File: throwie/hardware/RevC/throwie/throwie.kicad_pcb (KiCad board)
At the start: 2 copper layers, 33.8 x 18.8 mm, 24 parts, among them J1 CONN, Q1 2SC3356, Q2 SS8050-G, T1 TestPoints, T2 TestPoints, T3 TestPoints, T4 TestPoints, U1 C8051F850-A-GU, U2 MIC5231-3.3YM5-TR, X1 RO3101

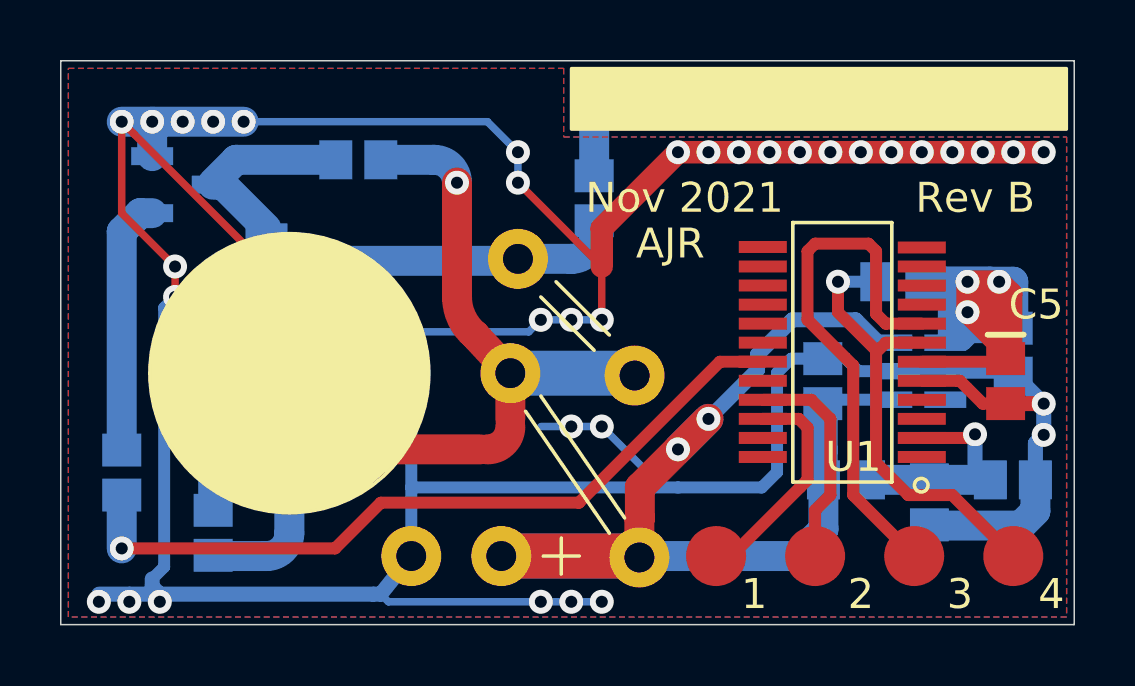
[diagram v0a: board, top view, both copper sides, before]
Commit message: added more test points
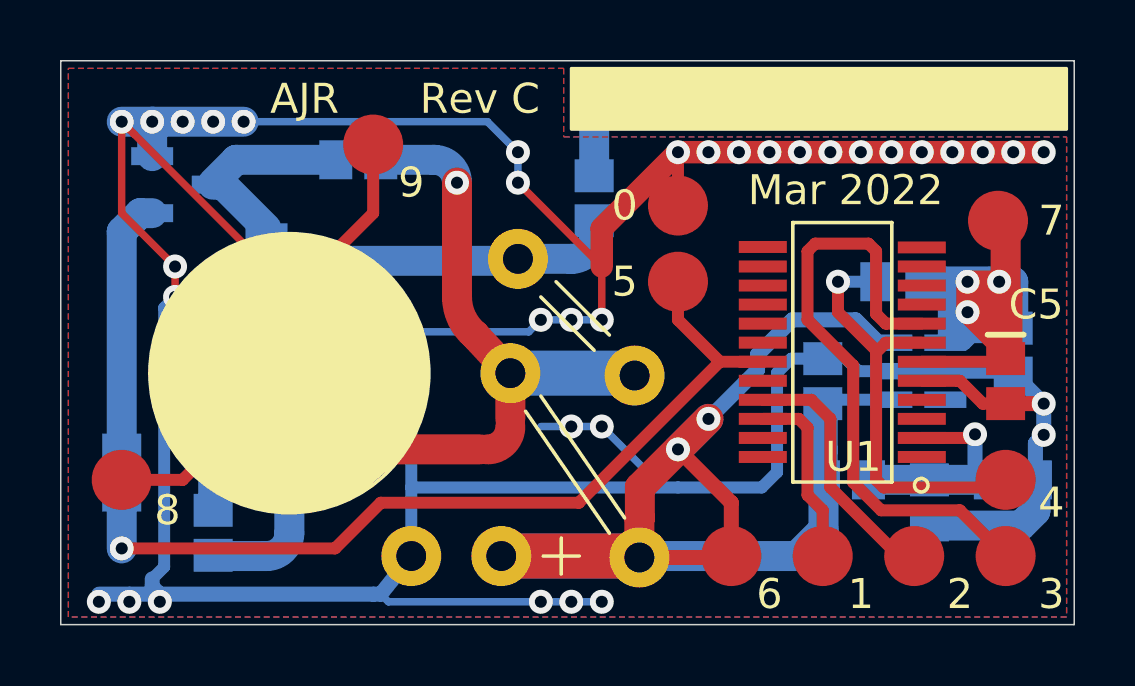
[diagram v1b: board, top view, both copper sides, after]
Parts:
- added T0: TestPoints, throwie:TestPoint, F.Cu at (41.1, 149.4)
- added T5: TestPoints, throwie:TestPoint, F.Cu at (41.1, 151.9)
- added T6: TestPoints, throwie:TestPoint, F.Cu at (42.9, 161.0)
- added T7: TestPoints, throwie:TestPoint, F.Cu at (51.8, 149.9)
- added T8: TestPoints, throwie:TestPoint, F.Cu at (22.6, 158.5)
- added T9: TestPoints, throwie:TestPoint, F.Cu at (31.0, 147.3)
- moved T1 3.56 mm to (46.0, 161.0)
- moved T2 3.30 mm to (49.0, 161.0)
- moved T4 3.05 mm to (52.1, 161.0)
- moved T3 2.55 mm to (52.1, 158.5)
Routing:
- net GNDREF: track 145.4 -> 160.4 mm
- net +BATT: track 40.1 -> 48.4 mm
- net +3V3: track 37.5 -> 42.2 mm
- net /MOD: track 27.5 -> 30.7 mm
- net Net-(T4-Pad1): track 17.9 -> 20.7 mm
- net Net-(T1-Pad1): track 7.45 -> 6.10 mm
- net Net-(T2-Pad1): track 7.30 -> 8.54 mm
- net Net-(R5-Pad2): track 15.6 -> 14.9 mm
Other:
- board text added: "0"
- board text added: "5"
- board text added: "6"
- board text added: "7"
- board text added: "8"
- board text added: "9"
- board text added: "Mar 2022"
- board text added: "Rev C"
- board text removed: "Nov 2021"
- board text removed: "Rev B"

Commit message: increase pads, update fab output
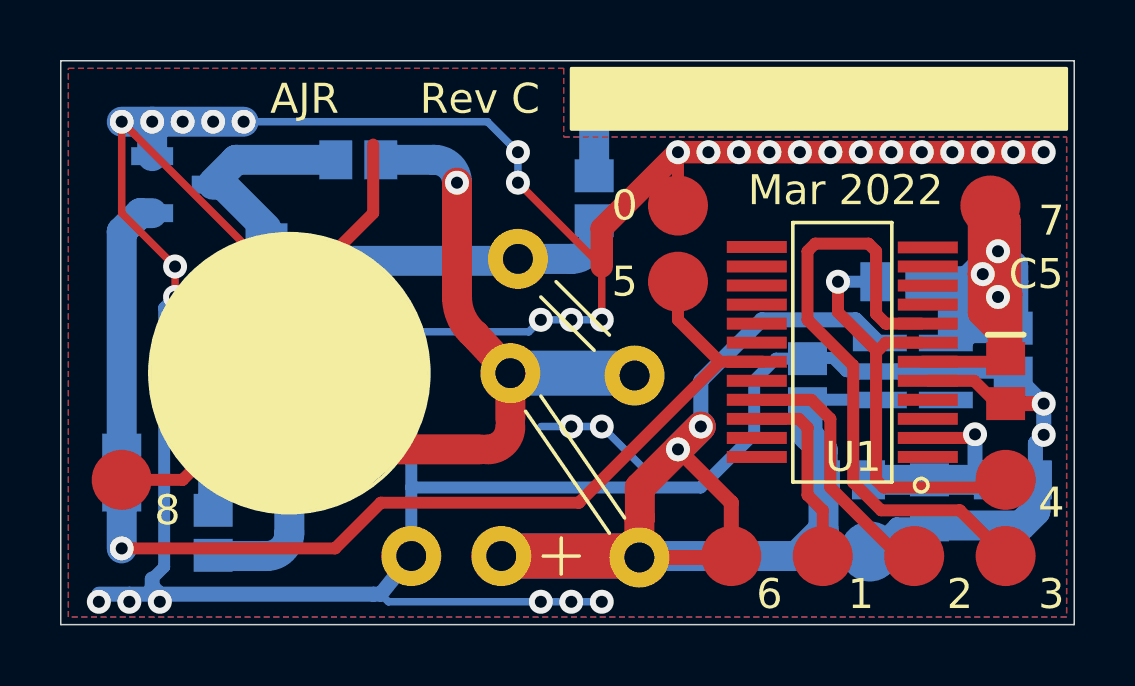
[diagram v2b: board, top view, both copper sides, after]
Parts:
- T9: moved to B.Cu
- moved T9 21.4 mm to (47.5, 160.9)
- moved T7 0.57 mm to (51.6, 149.4)
- moved C1 0.51 mm to (45.5, 156.0)
- moved U2 0.18 mm to (48.1, 153.9)
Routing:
- net +3V3: track 42.2 -> 51.3 mm
- net GNDREF: track 160.4 -> 161.2 mm
- net +BATT: track 48.4 -> 49.1 mm
